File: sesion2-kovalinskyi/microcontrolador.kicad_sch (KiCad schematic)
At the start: 0 parts

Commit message: Etapa de MCU completada
- MCU
- filtros RC
- resolución ERC con PWR_FLAG
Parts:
- added C3, C4: 100nF, Capacitor_SMD:C_0805_2012Metric, symbol Device:C
- added J2: Conn_01x06_Pin, Connector_PinHeader_2.54mm:PinHeader_1x06_P2.54mm_Vertical, symbol Connector:Conn_01x06_Pin
- added R1, R2: 1k, Resistor_SMD:R_0805_2012Metric, symbol Device:R
- added U2: ATmega328P-AU, Package_QFP:TQFP-32_7x7mm_P0.8mm, symbol MCU_Microchip_ATmega:ATmega328P-A
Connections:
- new net: J2.2 (Pin_2), R1.2
- new net: J2.3 (Pin_3), R2.2
- new net: J2.4 (Pin_4), U2.25 (PC2)
- new net: J2.5 (Pin_5), U2.26 (PC3)
- new net: C3.1, R1.1, U2.23 (PC0)
- new net: C4.1, R2.1, U2.24 (PC1)
- new net +3V3: J2.1 (Pin_1), U2.18 (AVCC), U2.4 (VCC), U2.6 (VCC)
- new net GND: C3.2, C4.2, J2.6 (Pin_6), U2.21 (GND), U2.3 (GND), U2.5 (GND)
- no-connect marks 0 -> 22

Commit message: Avance en layout y enrutado preliminar
- Enrutadas señales de datos, filtros y componentes pasivos.
- Implementados condensadores de desacoplo y test points (VIN, 3V3, GND).

Pendiente:
- Corregir asignación de ancho para pistas de alimentación (+3V3 a 0,5 mm).
- Validar conexiones a GND y cosido de vías con el plano inferior (B.Cu).
- Ejecutar DRC final y recálculo de zonas de relleno.
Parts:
- added C5, C6, C7: 100nF, Capacitor_SMD:C_0805_2012Metric, symbol Device:C
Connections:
- net +3V3: now also C5.1, C6.2
- net GND: now also C5.2, C6.1, C7.1
- net at U2.20 (AREF): now also C7.2
- no-connect marks 22 -> 21

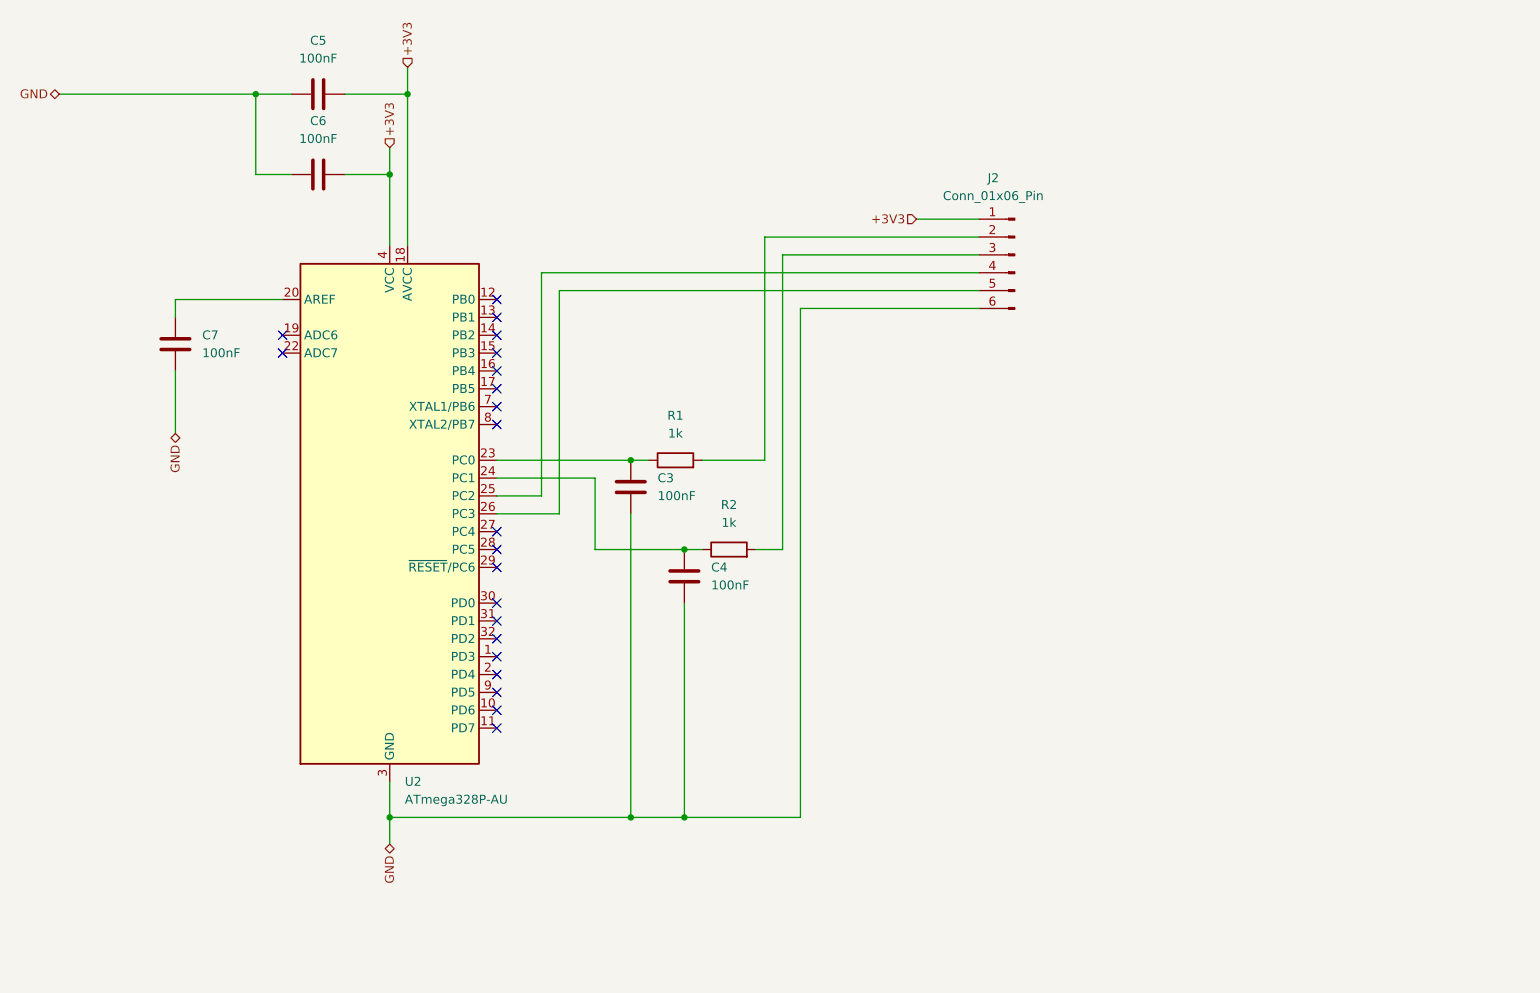
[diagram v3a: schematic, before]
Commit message: Calculo de impedancia y enrutado SPI e I2C
- I2C enrutado en Capa 3 (Stripline) con meandros (regla 3W) y desacoplo C8 pegado a los pines.
- SPI en Capa 1 con ajuste de longitud en SCK, MOSI y MISO (~25,35 mm) y puente en Capa 3 para SPI_CS.
- Validada la integridad de señal en los buses; líneas de datos libres de errores DRC.
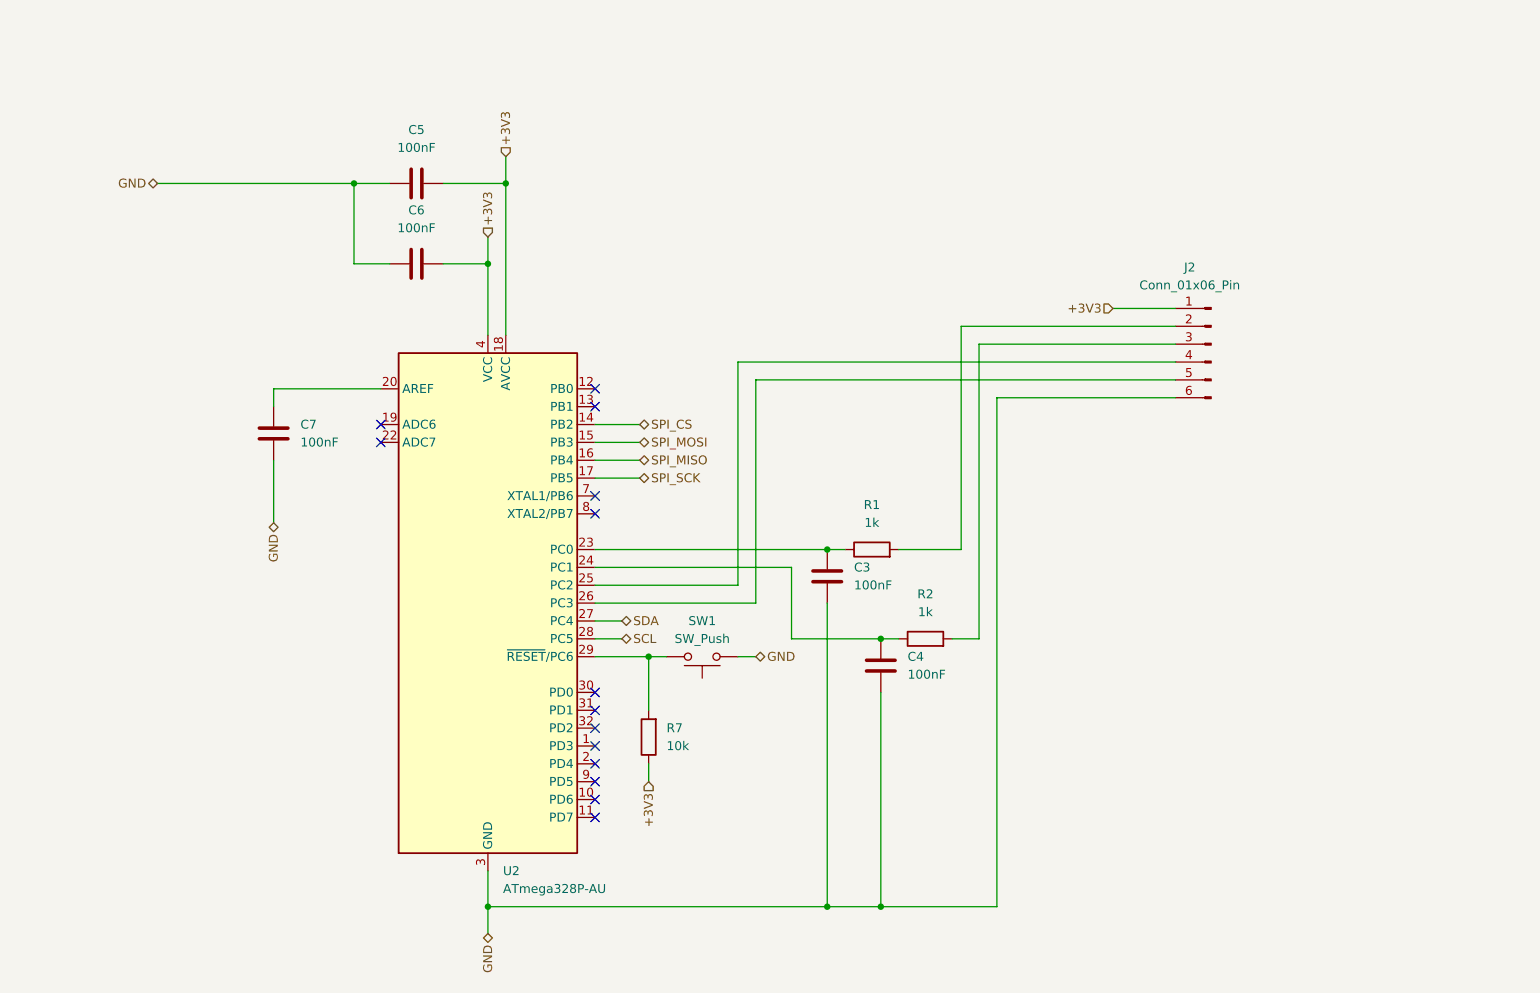
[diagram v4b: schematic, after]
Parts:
- added R7: 10k, Resistor_SMD:R_0805_2012Metric, symbol Device:R
- added SW1: SW_Push, Button_Switch_SMD:SW_SPST_TL3342, symbol Switch:SW_Push
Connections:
- net +3V3: now also R7.1
- net GND: now also SW1.1
- net SPI_CS: now reaches U2.14 (PB2)
- net SPI_MOSI: now reaches U2.15 (PB3)
- net SPI_MISO: now reaches U2.16 (PB4)
- net SPI_SCK: now reaches U2.17 (PB5)
- net SDA: now reaches U2.27 (PC4)
- net SCL: now reaches U2.28 (PC5)
- net at U2.29 (~{RESET}/PC6): now also R7.2, SW1.2
- no-connect marks 21 -> 14
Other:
- moved on the sheet: C3, C4, C5, C6, C7, J2, R1, R2, U2

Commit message: Sesión 4 - Entrega Completa
- Incorporación de dos sensores en el circuito: uno bajo protocolo I2C y otro bajo protocolo SPI.
- Integración física y esquemática de conector tipo USB-C para comunicación diferencial.
- Integrado bloque USB-C con CH340C y resuelto ERC (conectado el pin V3 a +3V3 según especifica el datasheet para operación a 3,3 V, excluyendo el falso positivo de conflicto de salidas de alimentación del ERC).
- Ajuste de par diferencial (DIFF_90): el uso directo de la herramienta "Tune Skew of Differential Pair" no computa la longitud total completa de las redes al existir saltos de vía y pistas auxiliares en el conector; por ello, el ajuste de longitud se ha resuelto mediante meandros manuales y la definición de reglas personalizadas para la verificación del skew intracanal (< 0.05 mm) en el DRC.
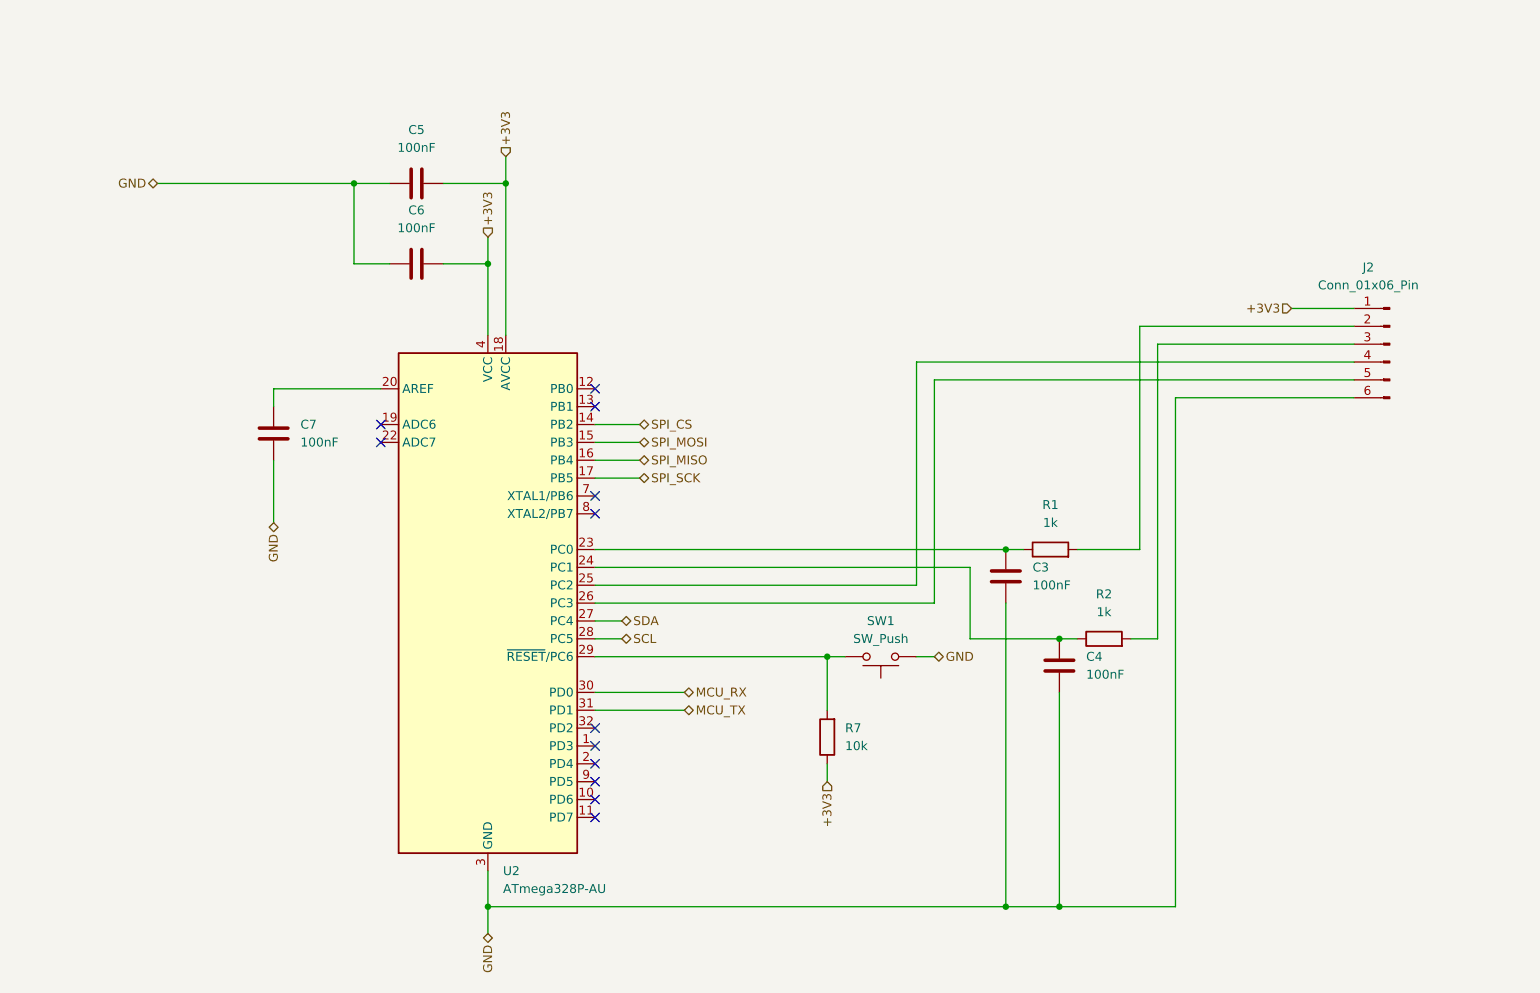
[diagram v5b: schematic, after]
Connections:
- net MCU_RX: now reaches U2.30 (PD0)
- net MCU_TX: now reaches U2.31 (PD1)
- no-connect marks 14 -> 12
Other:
- moved on the sheet: C3, C4, J2, R1, R2, R7, SW1

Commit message: Apartados 1 - 3 completados; integrando protecciones (apartado 4) en el esquemático
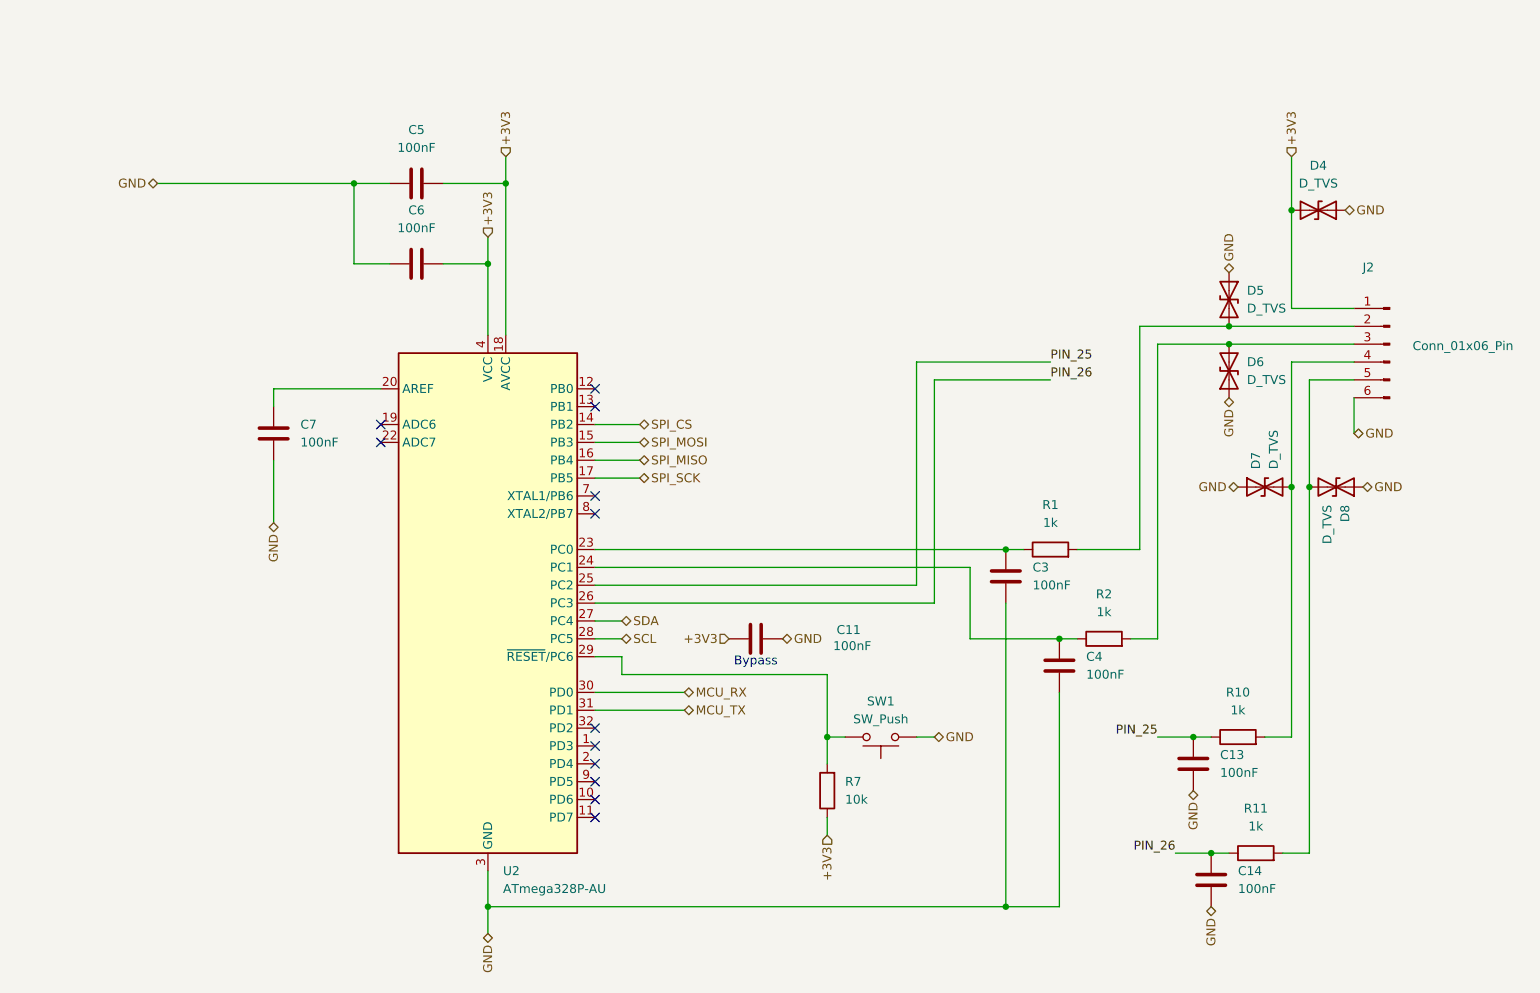
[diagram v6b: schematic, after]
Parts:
- added C11, C13, C14: 100nF, Capacitor_SMD:C_0805_2012Metric, symbol Device:C
- added D4, D5, D6, D7, D8: D_TVS, Diode_SMD:D_SOD-123, symbol Device:D_TVS
- added R10, R11: 1k, Resistor_SMD:R_0805_2012Metric, symbol Device:R
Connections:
- net +3V3: now also C11.1, D4.2 (A2)
- net GND: now also C11.2, C13.2, C14.2, D4.1 (A1), D5.1 (A1), D6.1 (A1), D7.1 (A1), D8.1 (A1)
- net at J2.2 (Pin_2), R1.2: now also D5.2 (A2)
- net at J2.3 (Pin_3), R2.2: now also D6.2 (A2)
- net at J2.4 (Pin_4): now also D7.2 (A2), R10.2; no longer U2.25 (PC2)
- net at J2.5 (Pin_5): now also D8.2 (A2), R11.2; no longer U2.26 (PC3)
- new net PIN_25: C13.1, R10.1, U2.25 (PC2)
- new net PIN_26: C14.1, R11.1, U2.26 (PC3)
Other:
- note added: "Bypass"
- moved on the sheet: R7, SW1

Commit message: Copia de seguridad Sesión 5
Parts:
- C11, C13, C14, C3, C4, C5, C6, C7: MPN (none) -> CC0805KRX7R9BB104
- D4, D5, D6, D7, D8: MPN (none) -> PESD3V3L1BA
- R1, R10, R11, R2: MPN (none) -> RC0805FR-071KL
- R7: MPN (none) -> RC0805FR-0710KL
- SW1: MPN (none) -> TL3342F160QG
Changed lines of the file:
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@@
+			)
+		)
+		(property "MPN" "CC0805KRX7R9BB104"
+			(at 219.71 138.43 0)
+			(hide yes)
+			(show_name no)
+			(do_not_autoplace no)
+			(effects
+				(font
+					(size 1.27 1.27)
+				)
 			)
 		)
@@
 			)
 		)
+		(property "MPN" "CC0805KRX7R9BB104"
+			(at 217.17 121.92 0)
+			(hide yes)
+			(show_name no)
+			(do_not_autoplace no)
+			(effects
+				(font
+					(size 1.27 1.27)
+				)
+			)
+		)
 		(pin "1"
 		)
@@
 			)
 		)
+		(property "MPN" "CC0805KRX7R9BB104"
+			(at 86.36 74.93 0)
+			(hide yes)
+			(show_name no)
+			(do_not_autoplace no)
+			(effects
+				(font
+					(size 1.27 1.27)
+				)
+			)
+		)
 		(pin "1"
 		)
@@
 			)
 		)
+		(property "MPN" "PESD3V3L1BA"
+			(at 234.95 43.18 0)
+			(hide yes)
+			(show_name no)
+			(do_not_autoplace no)
+			(effects
+				(font
+					(size 1.27 1.27)
+				)
+			)
+		)
 		(pin "2"
 		)
@@
 			)
 		)
+		(property "MPN" "RC0805FR-071KL"
+			(at 223.52 118.11 90)
+			(hide yes)
+			(show_name no)
+			(do_not_autoplace no)
+			(effects
+				(font
+					(size 1.27 1.27)
+				)
+			)
+		)
 		(pin "1"
 		)
@@
 			)
 		)
+		(property "MPN" "CC0805KRX7R9BB104"
+			(at 190.5 95.25 0)
+			(hide yes)
+			(show_name no)
+			(do_not_autoplace no)
+			(effects
+				(font
+					(size 1.27 1.27)
+				)
+			)
+		)
 		(pin "1"
 		)
@@
 			)
 		)
+		(property "MPN" "CC0805KRX7R9BB104"
+			(at 106.68 50.8 90)
+			(hide yes)
+			(show_name no)
+			(do_not_autoplace no)
+			(effects
+				(font
+					(size 1.27 1.27)
+				)
+			)
+		)
 		(pin "1"
 		)
@@
 			)
 		)
+		(property "MPN" "CC0805KRX7R9BB104"
+			(at 198.12 107.95 0)
+			(hide yes)
+			(show_name no)
+			(do_not_autoplace no)
+			(effects
+				(font
+					(size 1.27 1.27)
+				)
+			)
+		)
 		(pin "1"
 		)
@@
 			)
 		)
+		(property "MPN" "TL3342F160QG"
+			(at 172.72 118.11 0)
+			(hide yes)
+			(show_name no)
+			(do_not_autoplace no)
+			(effects
+				(font
+					(size 1.27 1.27)
+				)
+			)
+		)
 		(pin "2"
 		)
@@
 			)
 		)
+		(property "MPN" "PESD3V3L1BA"
+			(at 227.33 82.55 90)
+			(hide yes)
+			(show_name no)
+			(do_not_autoplace no)
+			(effects
+				(font
+					(size 1.27 1.27)
+				)
+			)
+		)
 		(pin "2"
 		)
@@
 			)
 		)
+		(property "MPN" "PESD3V3L1BA"
+			(at 237.49 82.55 90)
+			(hide yes)
+			(show_name no)
+			(do_not_autoplace no)
+			(effects
+				(font
+					(size 1.27 1.27)
+				)
+			)
+		)
 		(pin "2"
 		)
@@
 			)
 		)
+		(property "MPN" "RC0805FR-071KL"
+			(at 196.85 91.44 90)
+			(hide yes)
+			(show_name no)
+			(do_not_autoplace no)
+			(effects
+				(font
+					(size 1.27 1.27)
+				)
+			)
+		)
 		(pin "1"
 		)
@@
 		(property "Description" "Unpolarized capacitor"
 			(at 154.94 104.14 0)
+			(hide yes)
+			(show_name no)
+			(do_not_autoplace no)
+			(effects
+				(font
+					(size 1.27 1.27)
+				)
+			)
+		)
+		(property "MPN" "CC0805KRX7R9BB104"
+			(at 154.94 104.14 90)
 			(hide yes)
 			(show_name no)
@@
 			)
 		)
+		(property "MPN" "CC0805KRX7R9BB104"
+			(at 106.68 39.37 90)
+			(hide yes)
+			(show_name no)
+			(do_not_autoplace no)
+			(effects
+				(font
+					(size 1.27 1.27)
+				)
+			)
+		)
 		(pin "1"
 		)
@@
 			)
 		)
+		(property "MPN" "RC0805FR-071KL"
+			(at 204.47 104.14 90)
+			(hide yes)
+			(show_name no)
+			(do_not_autoplace no)
+			(effects
+				(font
+					(size 1.27 1.27)
+				)
+			)
+		)
 		(pin "1"
 		)
@@
 			)
 		)
+		(property "MPN" "PESD3V3L1BA"
+			(at 222.25 55.88 90)
+			(hide yes)
+			(show_name no)
+			(do_not_autoplace no)
+			(effects
+				(font
+					(size 1.27 1.27)
+				)
+			)
+		)
 		(pin "2"
 		)
@@
 			)
 		)
+		(property "MPN" "PESD3V3L1BA"
+			(at 222.25 66.04 90)
+			(hide yes)
+			(show_name no)
+			(do_not_autoplace no)
+			(effects
+				(font
+					(size 1.27 1.27)
+				)
+			)
+		)
 		(pin "2"
 		)
@@
 			)
 		)
+		(property "MPN" "RC0805FR-071KL"
+			(at 226.06 134.62 90)
+			(hide yes)
+			(show_name no)
+			(do_not_autoplace no)
+			(effects
+				(font
+					(size 1.27 1.27)
+				)
+			)
+		)
 		(pin "1"
 		)
@@
 			(at 165.1 125.73 0)
 			(hide yes)
+			(show_name no)
+			(do_not_autoplace no)
+			(effects
+				(font
+					(size 1.27 1.27)
+				)
+			)
+		)
+		(property "MPN" "RC0805FR-0710KL"
+			(at 165.1 125.73 0)
+			(hide yes)
